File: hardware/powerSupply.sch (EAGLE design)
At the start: 94 parts, among them IC1 MCP3008, IC12 LM358, IC2 LM334Z, IC3 MCP4821P, IC4 MCP4821P, IC5 74LS139D, IC6 7805TV, IC7 LP2950Z, IC8 LT3080T, IC9 LM358, J3 RASPBERRYPI-40-PIN-GPIO_PTH, SW1 EC11B_SW, SW2 EC11B_SW, SW7 B3F-1000, T1 2N3904, T3 2N3904, U1 MAX874CPA, X1 VOUT, X2 VSENSE, X3 VIN

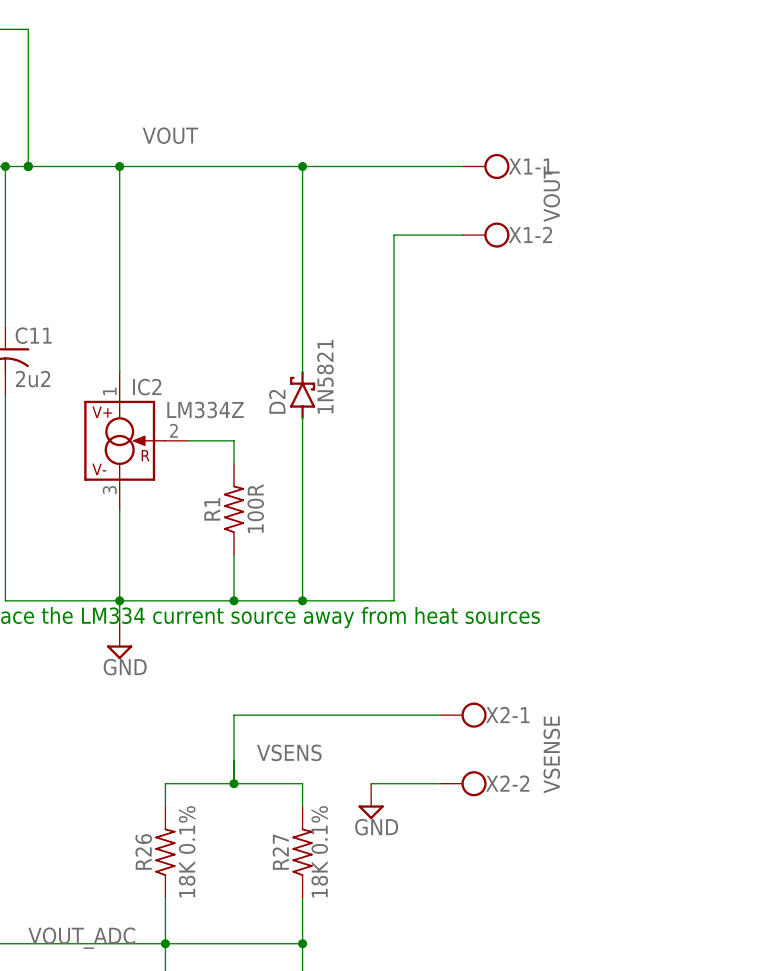
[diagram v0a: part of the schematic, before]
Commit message: 
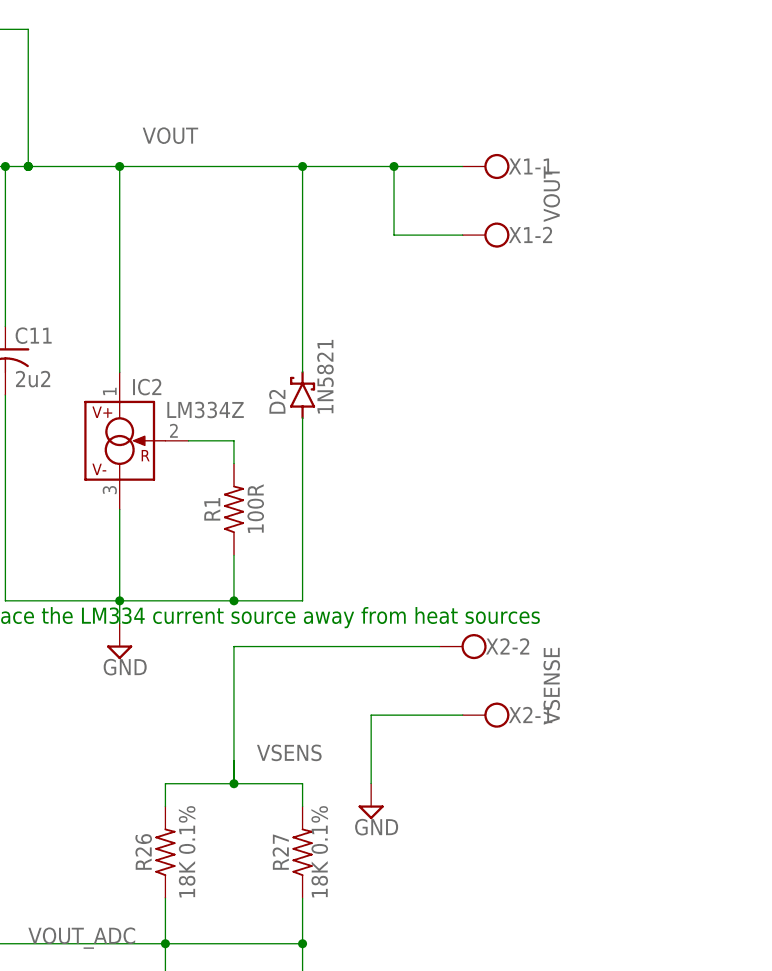
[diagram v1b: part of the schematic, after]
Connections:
- net V+1 renamed VR
- net GND: now also X2-1.KL; no longer X1-2.KL, X2-2.KL
- net VOUT: now also X1-2.KL
- net VSENS: now also X2-2.KL; no longer X2-1.KL
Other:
- moved on the sheet: X2-1, X2-2
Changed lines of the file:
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@@
 <attribute name="NAME" x="337.82" y="159.131" size="1.778" layer="95"/>
 </instance>
-<instance part="X2" gate="-1" x="335.28" y="106.68" smashed="yes" rot="R180" grouprefs="REGULATOR">
-<attribute name="NAME" x="335.28" y="105.791" size="1.778" layer="95"/>
-</instance>
-<instance part="X2" gate="-2" x="335.28" y="99.06" smashed="yes" rot="R180" grouprefs="REGULATOR">
-<attribute name="VALUE" x="341.757" y="106.68" size="1.778" layer="96" rot="R270"/>
-<attribute name="NAME" x="335.28" y="98.171" size="1.778" layer="95"/>
+<instance part="X2" gate="-1" x="337.82" y="106.68" smashed="yes" rot="R180" grouprefs="REGULATOR">
+<attribute name="NAME" x="337.82" y="105.791" size="1.778" layer="95"/>
+</instance>
+<instance part="X2" gate="-2" x="335.28" y="114.3" smashed="yes" rot="R180" grouprefs="REGULATOR">
+<attribute name="VALUE" x="341.757" y="114.3" size="1.778" layer="96" rot="R270"/>
+<attribute name="NAME" x="335.28" y="113.411" size="1.778" layer="95"/>
 </instance>
 <instance part="X3" gate="-1" x="-22.86" y="182.88" smashed="yes" grouprefs="CURRENT_MONITOR">
@@
 <junction x="314.96" y="167.64"/>
 <label x="297.18" y="170.18" size="1.778" layer="95"/>
-<wire x1="332.74" y1="167.64" x2="314.96" y2="167.64" width="0.1524" layer="91"/>
+<wire x1="332.74" y1="167.64" x2="325.12" y2="167.64" width="0.1524" layer="91"/>
+<wire x1="325.12" y1="167.64" x2="314.96" y2="167.64" width="0.1524" layer="91"/>
 <wire x1="281.94" y1="149.86" x2="281.94" y2="167.64" width="0.1524" layer="91"/>
 <junction x="281.94" y="167.64"/>
 <pinref part="C11" gate="G$1" pin="+"/>
 <pinref part="X1" gate="-1" pin="KL"/>
+<pinref part="X1" gate="-2" pin="KL"/>
+<wire x1="332.74" y1="160.02" x2="325.12" y2="160.02" width="0.1524" layer="91"/>
+<wire x1="325.12" y1="160.02" x2="325.12" y2="167.64" width="0.1524" layer="91"/>
+<junction x="325.12" y="167.64"/>
 </segment>
 </net>
@@
 <wire x1="294.64" y1="116.84" x2="294.64" y2="119.38" width="0.1524" layer="91"/>
 <junction x="294.64" y="119.38"/>
-<wire x1="332.74" y1="160.02" x2="325.12" y2="160.02" width="0.1524" layer="91"/>
-<wire x1="325.12" y1="160.02" x2="325.12" y2="119.38" width="0.1524" layer="91"/>
-<wire x1="325.12" y1="119.38" x2="314.96" y2="119.38" width="0.1524" layer="91"/>
-<junction x="314.96" y="119.38"/>
 <wire x1="281.94" y1="142.24" x2="281.94" y2="119.38" width="0.1524" layer="91"/>
 <pinref part="C11" gate="G$1" pin="-"/>
-<pinref part="X1" gate="-2" pin="KL"/>
 </segment>
 <segment>
@@
 <pinref part="SUPPLY8" gate="GND" pin="GND"/>
 <wire x1="175.26" y1="55.88" x2="175.26" y2="27.94" width="0.1524" layer="91" grouprefs="VI_SET"/>
-</segment>
-<segment>
-<pinref part="SUPPLY9" gate="GND" pin="GND"/>
-<pinref part="X2" gate="-2" pin="KL"/>
-<wire x1="322.58" y1="99.06" x2="330.2" y2="99.06" width="0.1524" layer="91"/>
 </segment>
 <segment>
@@
 <pinref part="JP2" gate="A" pin="5"/>
 <wire x1="330.2" y1="-40.64" x2="340.36" y2="-40.64" width="0.1524" layer="91"/>
+</segment>
+<segment>
+<pinref part="SUPPLY9" gate="GND" pin="GND"/>
+<wire x1="322.58" y1="99.06" x2="322.58" y2="106.68" width="0.1524" layer="91"/>
+<pinref part="X2" gate="-1" pin="KL"/>
+<wire x1="322.58" y1="106.68" x2="332.74" y2="106.68" width="0.1524" layer="91"/>
 </segment>
 </net>
@@
 <junction x="307.34" y="99.06"/>
 <label x="309.88" y="101.6" size="1.778" layer="95"/>
-<wire x1="307.34" y1="99.06" x2="307.34" y2="106.68" width="0.1524" layer="91"/>
-<wire x1="307.34" y1="106.68" x2="330.2" y2="106.68" width="0.1524" layer="91"/>
-<pinref part="X2" gate="-1" pin="KL"/>
+<pinref part="X2" gate="-2" pin="KL"/>
+<wire x1="307.34" y1="99.06" x2="307.34" y2="114.3" width="0.1524" layer="91"/>
+<wire x1="307.34" y1="114.3" x2="330.2" y2="114.3" width="0.1524" layer="91"/>
 </segment>
 </net>
@@
 </segment>
 </net>
-<net name="V+1" class="0">
+<net name="VR" class="0">
 <segment>
 <wire x1="104.14" y1="177.8" x2="104.14" y2="180.34" width="0.1524" layer="91"/>
